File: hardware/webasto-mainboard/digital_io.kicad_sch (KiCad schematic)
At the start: 53 parts, among them Q10 2N7002, Q11 2N7002, Q12 SSM3J374R, Q13 2N7002, Q14 SUD50P04-08, Q15 SUD50P04-08, Q16 SUD50P04-08, Q17 SUD50P04-08, Q18 SUD50P04-08, Q2 2N7002, Q3 2N7002, Q4 2N7002, Q5 2N7002, Q6 SUD50P04-08, Q7 SUD50P04-08, Q8 SUD50P04-08, Q9 SUD50P04-08, U4 LM7805_TO220, U5 MC33660BEFR2, U6 INA219BxDCN

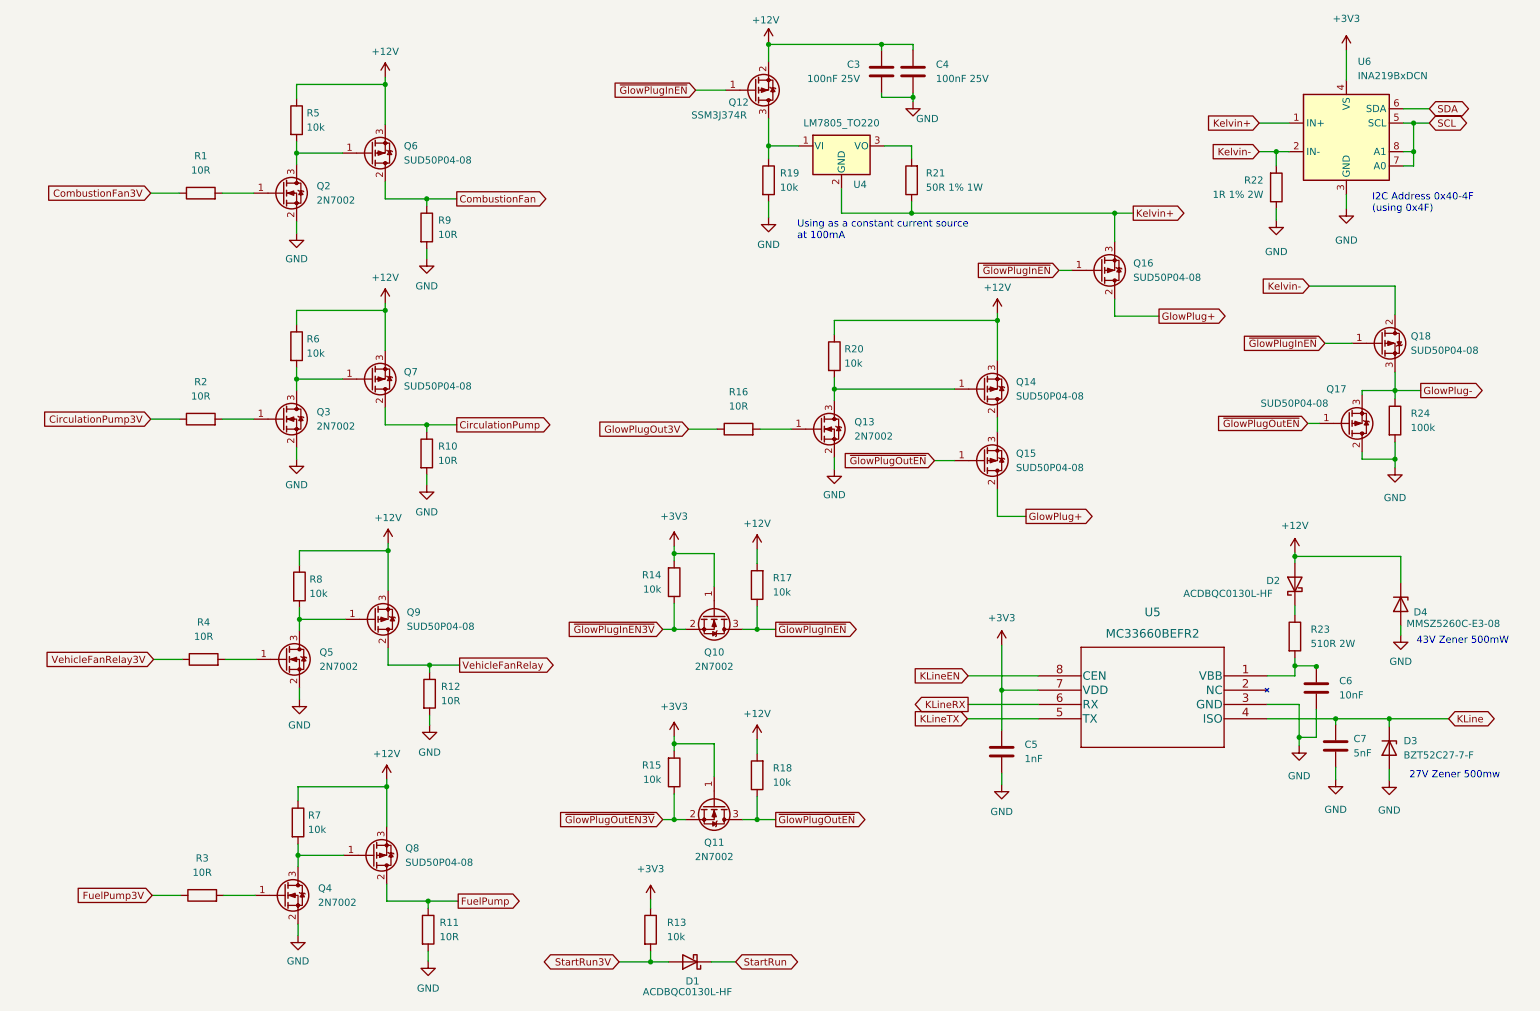
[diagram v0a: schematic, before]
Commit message: Added EmergencyStop input.  Hope I never need it.
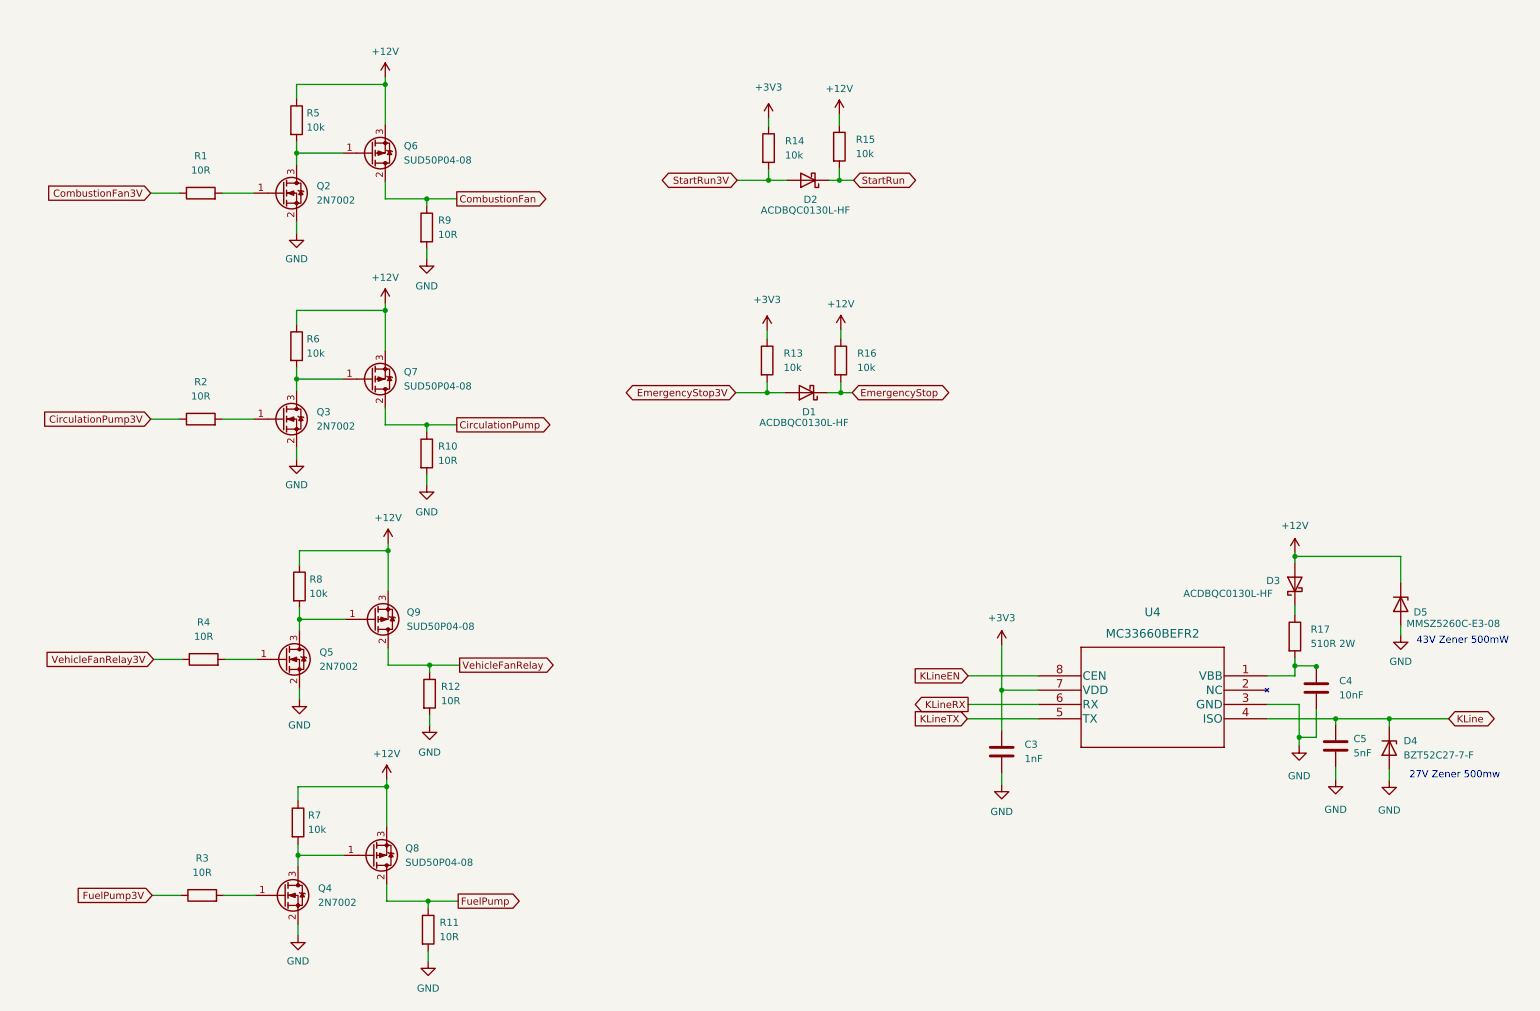
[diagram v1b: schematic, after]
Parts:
- removed C3: 100nF 25V, Capacitor_SMD:C_0805_2012Metric_Pad1.18x1.45mm_HandSolder, symbol Device:C
- removed C4: 100nF 25V, Capacitor_SMD:C_0603_1608Metric_Pad1.08x0.95mm_HandSolder, symbol Device:C
- removed Q10, Q11, Q13: 2N7002, Package_TO_SOT_SMD:SOT-23, symbol Transistor_FET:2N7002
- removed Q12: SSM3J374R, Package_TO_SOT_SMD:SOT-23, symbol Transistor_FET:AO3401A
- removed Q14, Q15, Q16, Q17, Q18: SUD50P04-08, Package_TO_SOT_SMD:TO-252-2, symbol Transistor_FET:SUD50P04-08
- removed R14, R17, R18, R19, R20: 10k, Resistor_SMD:R_0805_2012Metric_Pad1.20x1.40mm_HandSolder, symbol Device:R
- removed R21: 50R 1% 1W, Resistor_SMD:R_2816_7142Metric_Pad3.20x4.45mm_HandSolder, symbol Device:R
- removed R22: 1R 1% 2W, Resistor_SMD:R_2512_6332Metric_Pad1.40x3.35mm_HandSolder, symbol Device:R
- removed R24: 100k, Resistor_SMD:R_0805_2012Metric_Pad1.20x1.40mm_HandSolder, symbol Device:R
- removed U4: LM7805_TO220, Package_TO_SOT_THT:TO-220-3_Vertical, symbol Regulator_Linear:LM7805_TO220
- removed U6: INA219BxDCN, Package_TO_SOT_SMD:SOT-23-8, symbol Analog_ADC:INA219BxDCN
- added D1: ACDBQC0130L-HF, Diode_SMD:D_SOD-923, symbol Device:D_Schottky
- added R13: 10k, Resistor_SMD:R_0805_2012Metric_Pad1.20x1.40mm_HandSolder, symbol Device:R
- R16: value 10R -> 10k
- renumbered C5 to C3, C6 to C4, C7 to C5, D1 to D2, D2 to D3, D3 to D4, D4 to D5, R13 to R14, R23 to R17, U5 to U4
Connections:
- net GlowPlugOut3V is gone; now on net +12V: R16.1
- net ~{GlowPlugOutEN3V} is gone; now on net +12V: R15.1
- net +3V3: now also R13.1; no longer R15.2
- net StartRun: now also R15.2
- net EmergencyStop: now reaches R16.2
- net EmergencyStop: now also D1.1 (K)
- new net EmergencyStop3V: D1.2 (A), R13.2
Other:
- note removed: "I2C Address 0x40-4F (using 0x4F)"
- note removed: "Using as a constant current source at 100mA"
- moved on the sheet: D2, R14

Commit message: Oops.  StartRun is active at +12V.  Change the level translation.
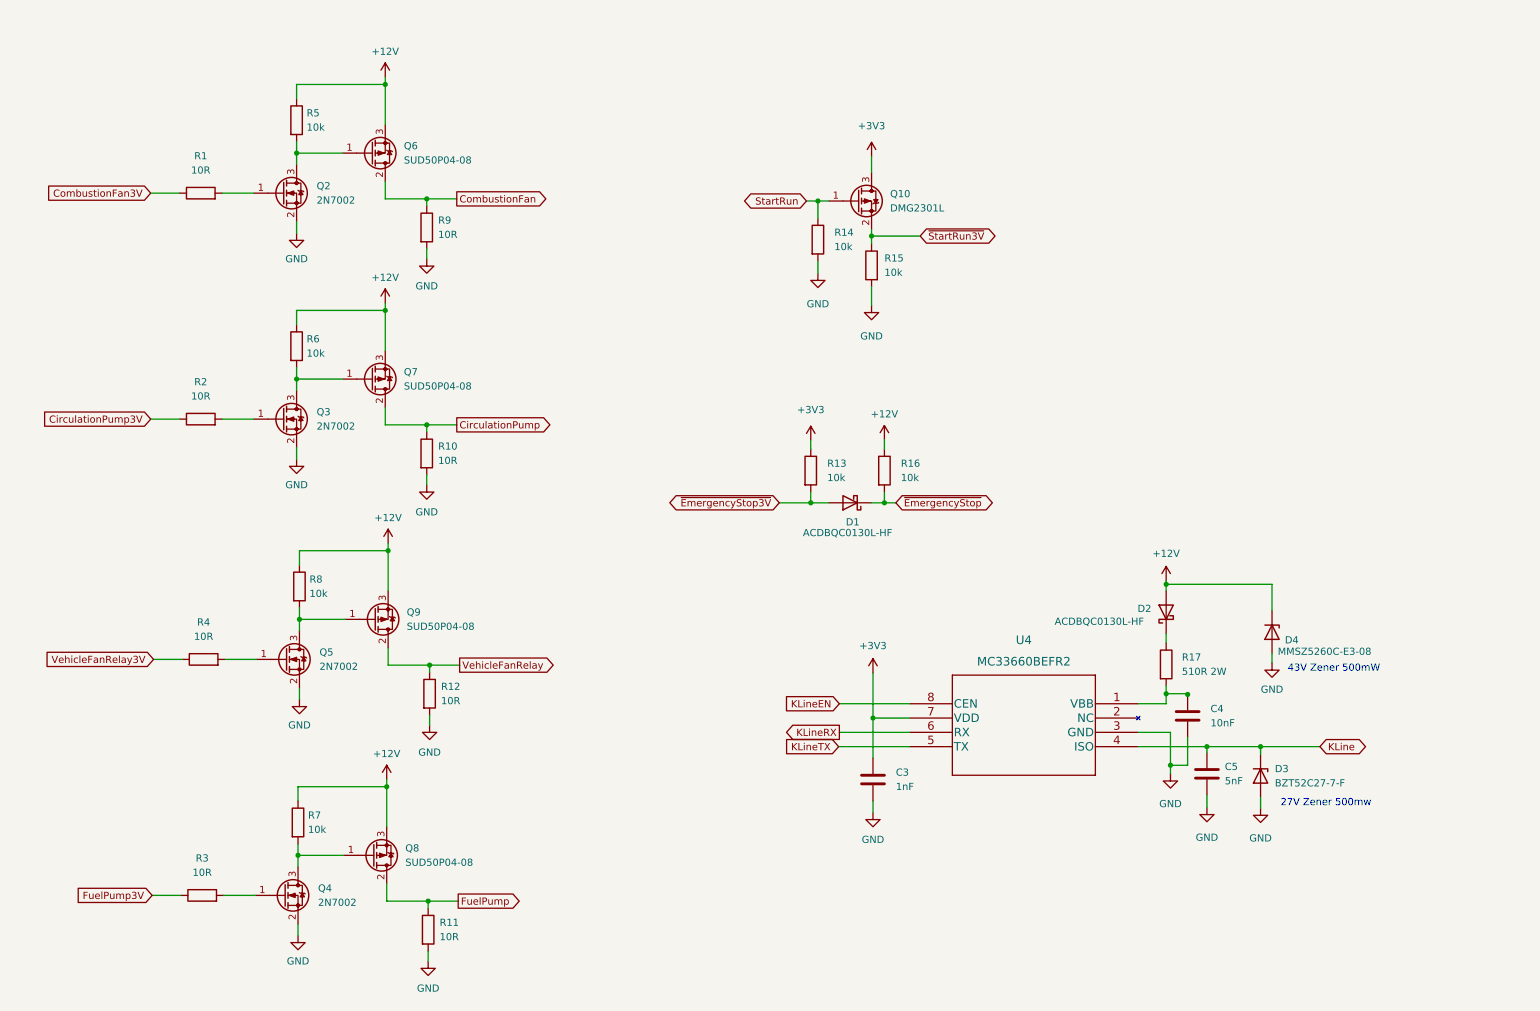
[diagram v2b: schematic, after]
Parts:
- removed D2: ACDBQC0130L-HF, Diode_SMD:D_SOD-923, symbol Device:D_Schottky
- added Q10: DMG2301L, Package_TO_SOT_SMD:SOT-23, symbol Transistor_FET:DMG2301L
- renumbered D3 to D2, D4 to D3, D5 to D4, R15 to R14, R14 to R15
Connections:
- net StartRun3V is gone; now on net GND: R15.2
- net +12V: no longer R14.1
- net +3V3: now also Q10.3 (D); no longer R15.1
- net GND: now also R14.2
- net StartRun: now also R14.1, Q10.1 (G); no longer R14.2
- net EmergencyStop renamed ~{EmergencyStop}
- net EmergencyStop3V renamed ~{EmergencyStop3V}
- new net ~{StartRun3V}: Q10.2 (S), R15.1
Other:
- moved on the sheet: C3, C4, C5, D1, D2, D3, D4, R13, R14, R15, R16, R17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

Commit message: Added the LEDs onto the board and init
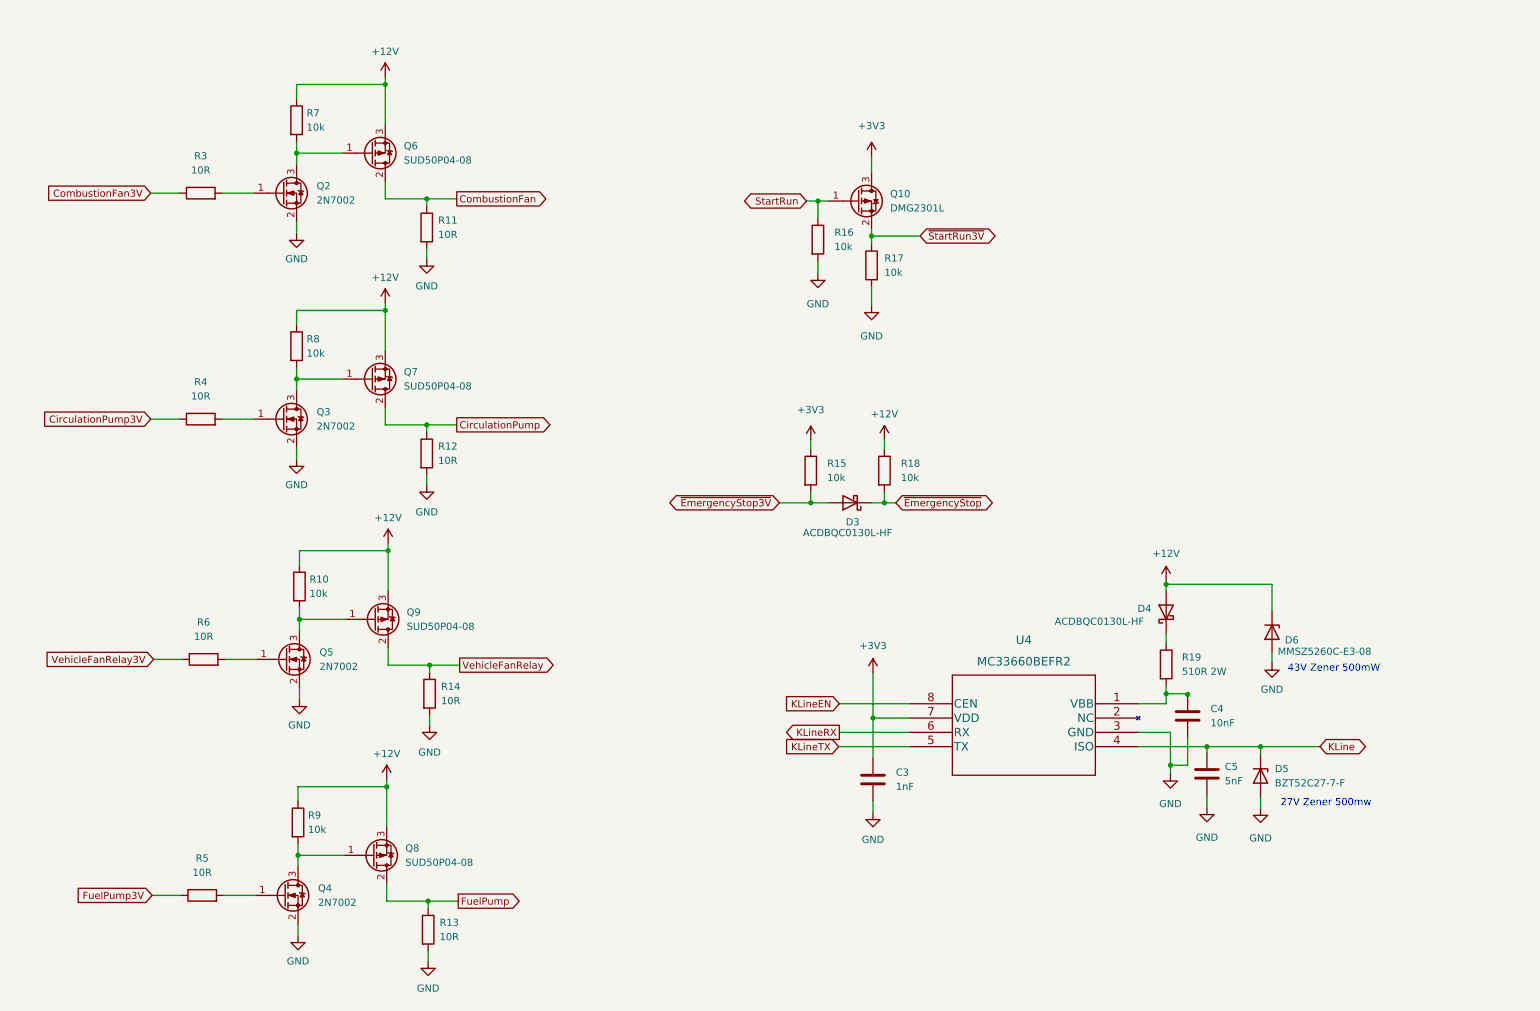
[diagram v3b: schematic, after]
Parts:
- renumbered D1 to D3, D2 to D4, D3 to D5, D4 to D6, R8 to R10, R9 to R11, R10 to R12, R11 to R13, R12 to R14, R13 to R15, R14 to R16, R15 to R17, R16 to R18, R17 to R19, R1 to R3, R2 to R4, R3 to R5, R4 to R6, R5 to R7, R6 to R8, R7 to R9

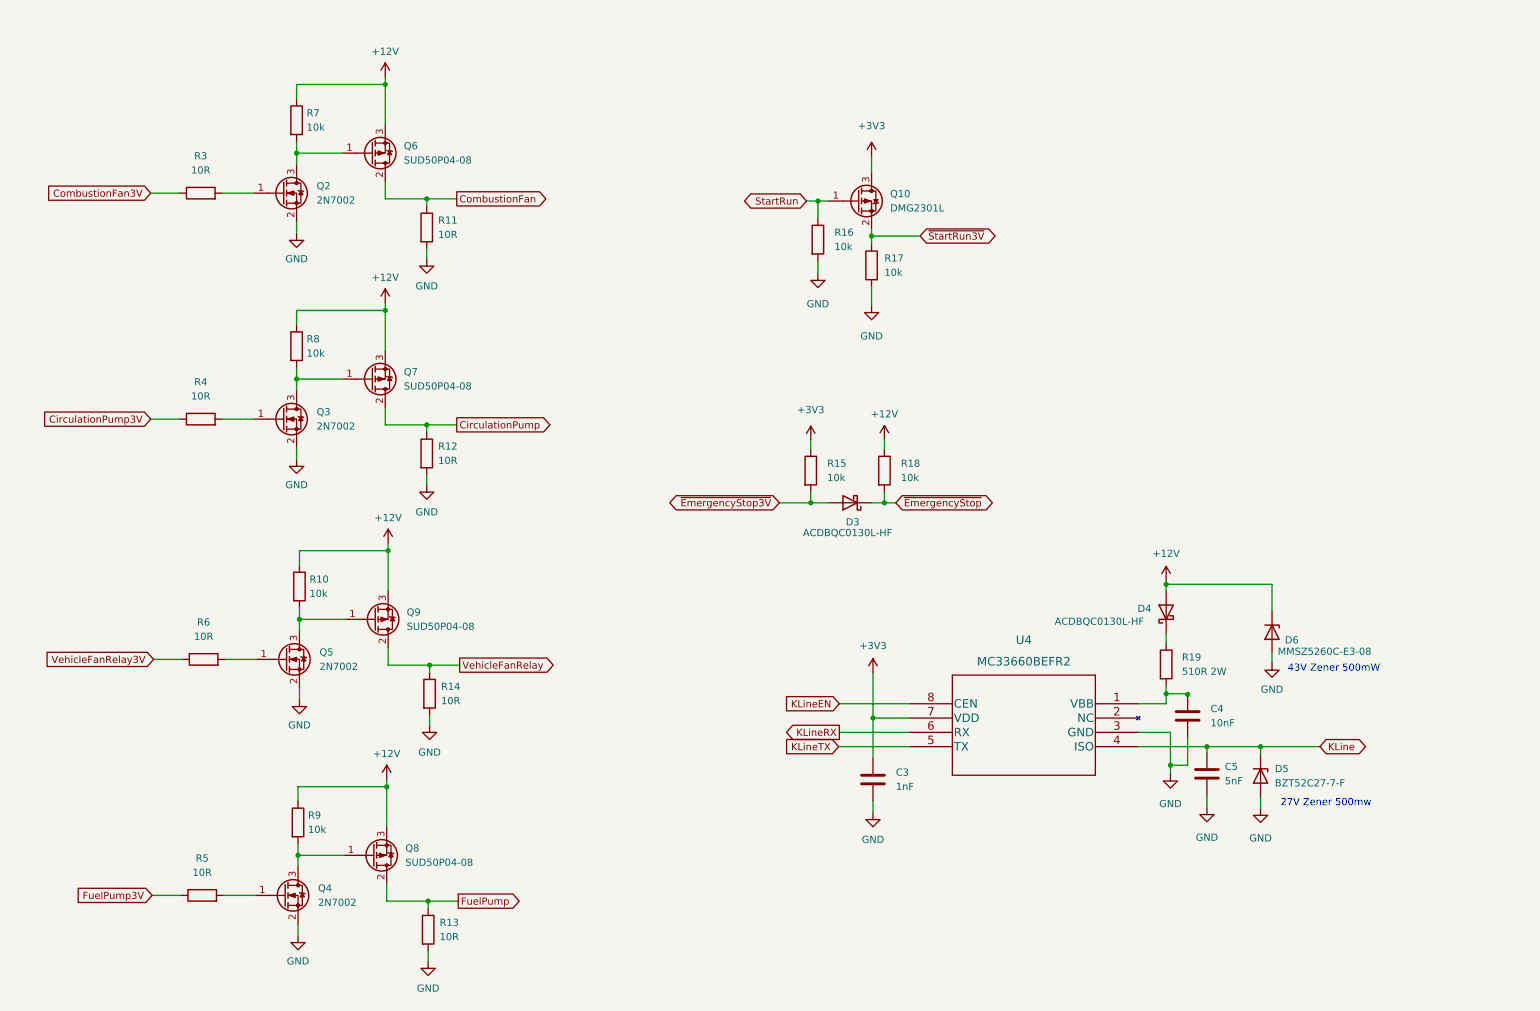
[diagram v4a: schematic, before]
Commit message: Added "USE_USB" input to choose console
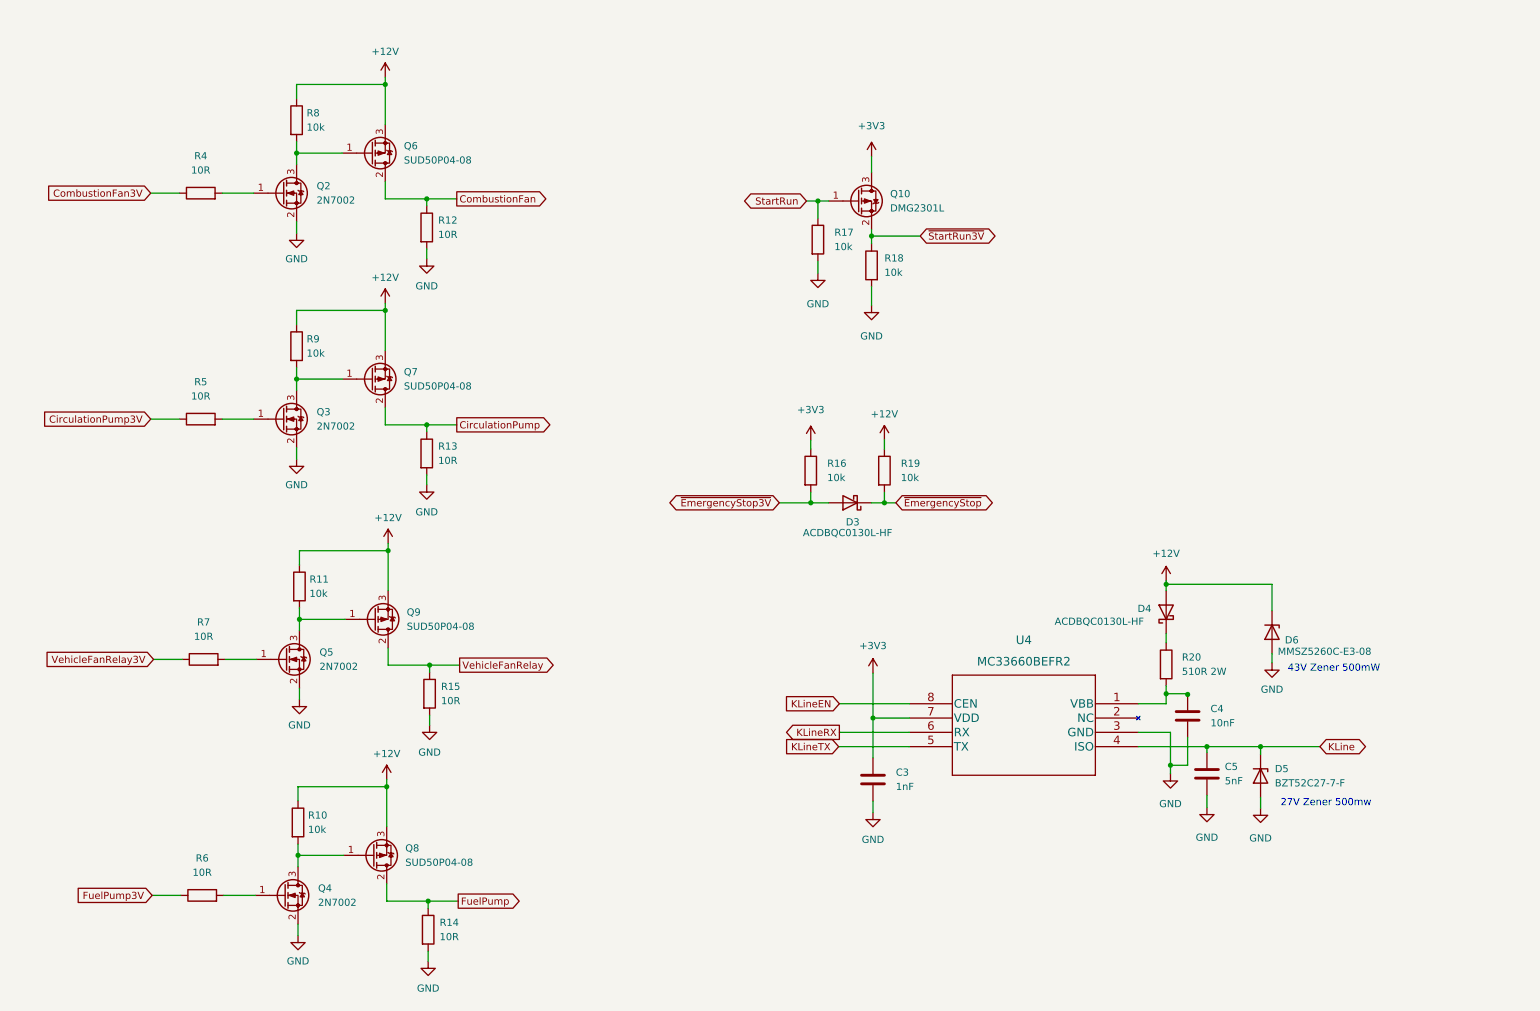
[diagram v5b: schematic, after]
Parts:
- renumbered R9 to R10, R10 to R11, R11 to R12, R12 to R13, R13 to R14, R14 to R15, R15 to R16, R16 to R17, R17 to R18, R18 to R19, R19 to R20, R3 to R4, R4 to R5, R5 to R6, R6 to R7, R7 to R8, R8 to R9
